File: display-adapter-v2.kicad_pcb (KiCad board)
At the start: 2 copper layers, 70 x 38 mm, 9 parts, among them J1 Display_In, J2 Inky_Left_1_20, J3 Inky_Right_21_40, J4 Display_Out_2, J5 Display_Out_3, J6 Display_Out_4

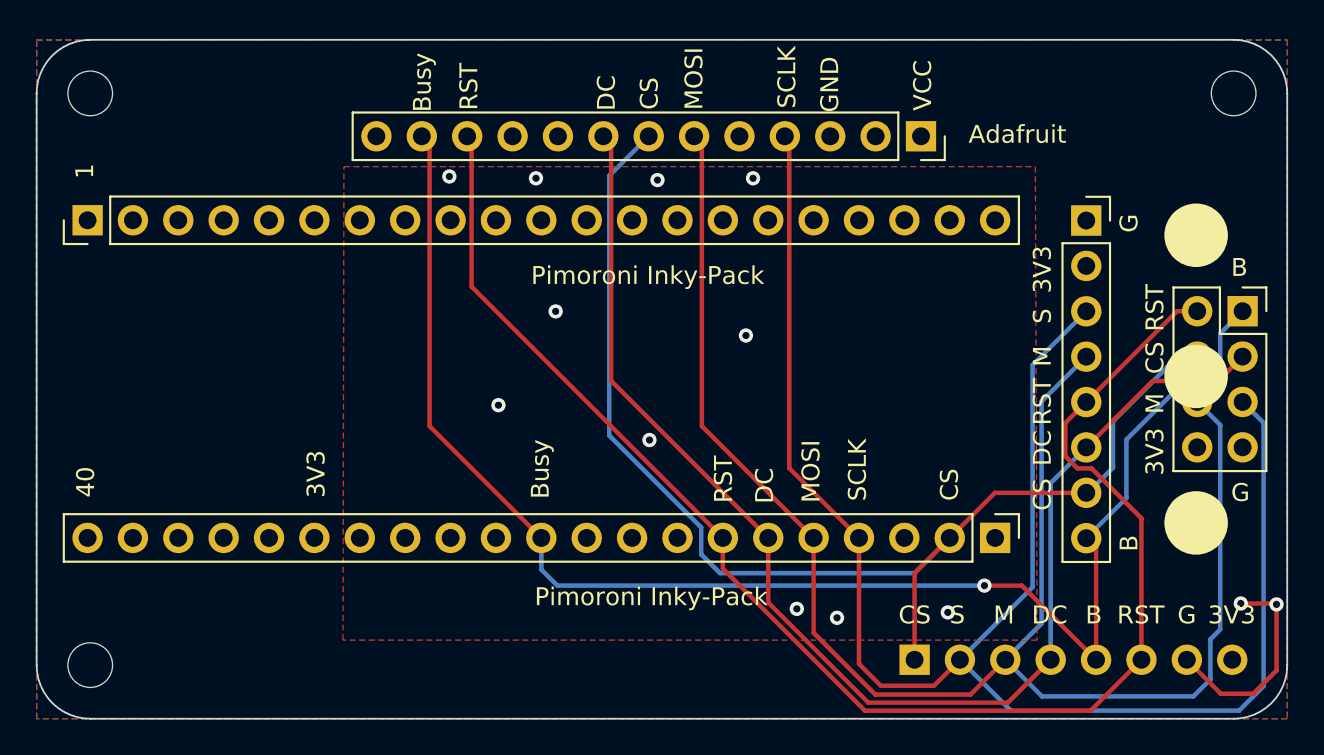
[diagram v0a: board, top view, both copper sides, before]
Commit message: bugfix: wrong 1x21 instead of 1x20 footprint for Inky-connectors
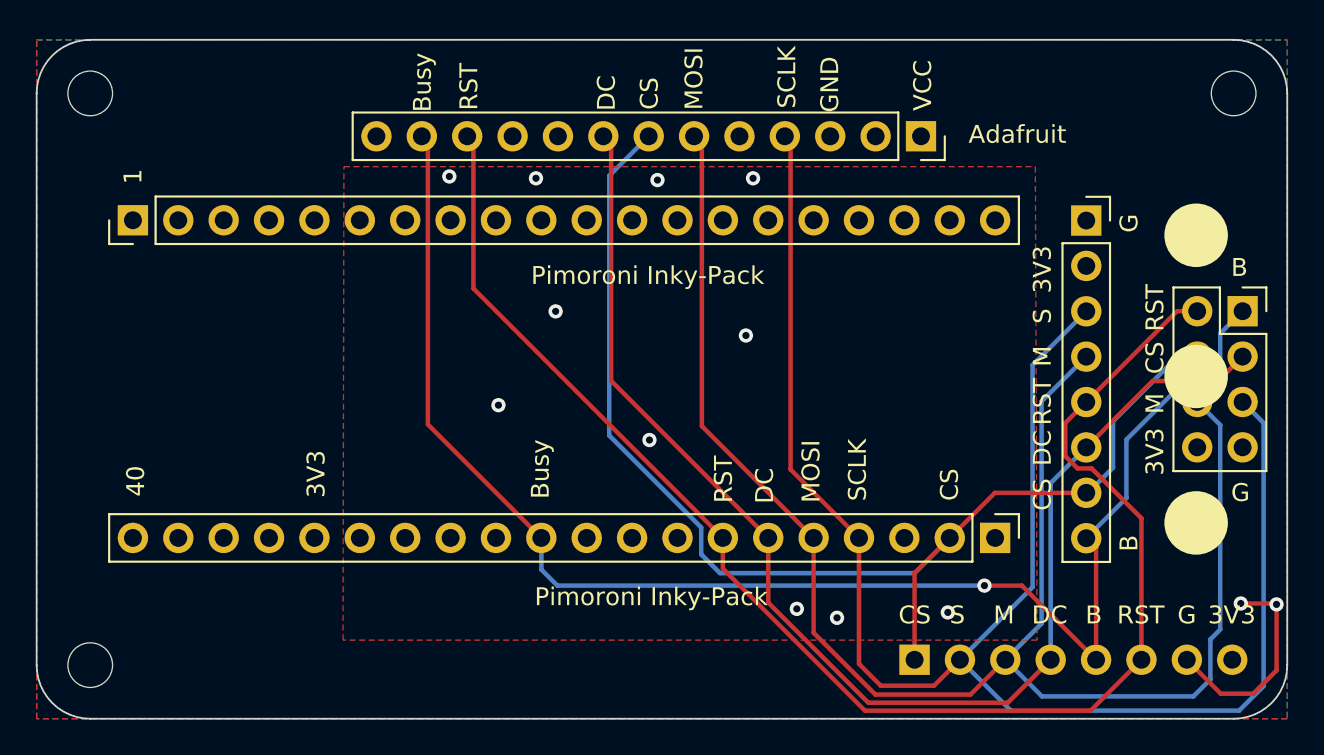
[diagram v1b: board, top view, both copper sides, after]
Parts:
- J2, J3: footprint Connector_PinHeader_2.54mm:PinHeader_1x21_P2.54mm_Vertical -> Connector_PinHeader_2.54mm:PinHeader_1x20_P2.54mm_Vertical
- moved J2 2.54 mm to (105.4, 110.1)
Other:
- board text added: "https://github.com/bablokb/pcb-datalogger-display-adapter-v2 Display Adapter V2 Rev. 1.01"
- board text removed: "https://github.com/bablokb/pcb-datalogger-display-adapter-v2 Display Adapter V2 Rev. 1.00"
